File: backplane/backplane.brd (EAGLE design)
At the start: 177 x 80 mm, 10 parts, among them J1 09232486825, J10 TB009-508-05BE, J2 09232486825, J3 09232486825, J4 09232486825, J5 09232486825, J6 09232486825, J7 09232486825, J8 09232486825

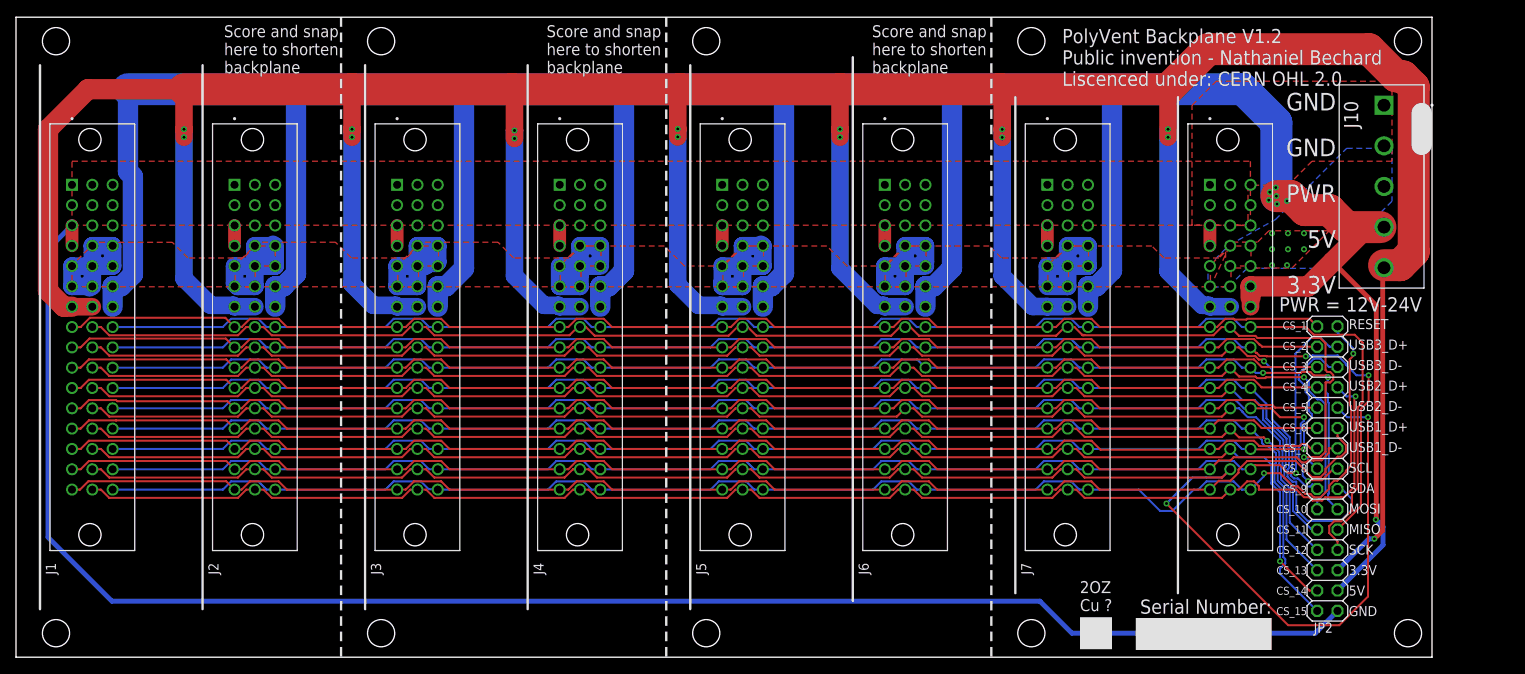
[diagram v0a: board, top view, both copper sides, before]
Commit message: added even wider traces to the backplane
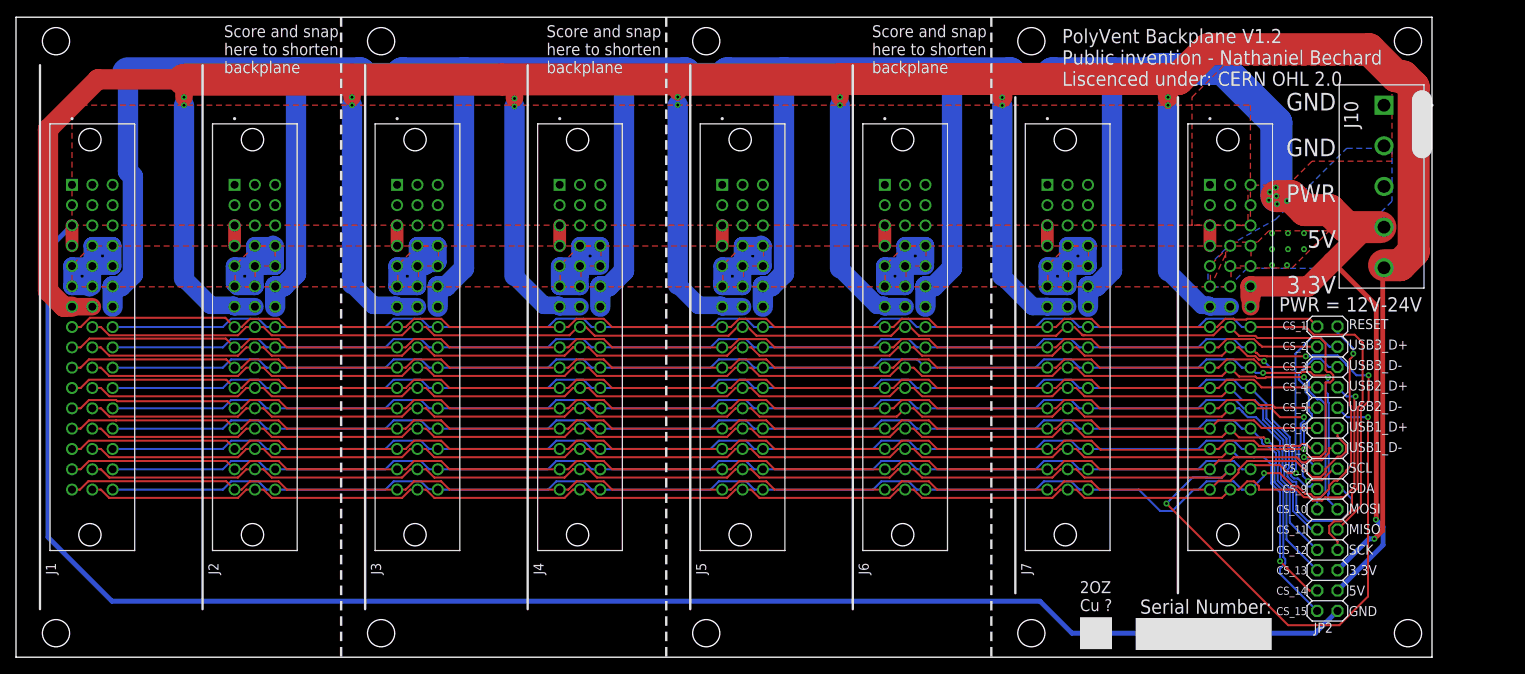
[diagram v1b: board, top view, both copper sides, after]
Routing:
- net 5V: track 447.8 -> 464.9 mm
- net 3.3V: track 510.2 -> 516.6 mm
